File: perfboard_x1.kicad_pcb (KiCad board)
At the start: 2 copper layers, 107.1 x 81.3 mm, 121 parts, among them J1 Conn_01x10, J10 Conn_01x10, J100 Conn_01x10, J101 Conn_01x10, J102 Conn_01x10, J103 Conn_01x10, J104 Conn_01x10, J105 Conn_01x10, J106 Conn_01x10, J107 Conn_01x10, J108 Conn_01x10, J109 Conn_01x10, J11 Conn_01x10, J110 Conn_01x10, J111 Conn_01x10, J112 Conn_01x10, J113 Conn_01x10, J114 Conn_01x10, J115 Conn_01x10, J116 Conn_01x10, J117 Conn_01x10, J118 Conn_01x10, J119 Conn_01x10, J12 Conn_01x10, J120 Conn_01x10, J13 Conn_01x10, J14 Conn_01x10, J15 Conn_01x10, J16 Conn_01x10, J17 Conn_01x10, J18 Conn_01x10, J19 Conn_01x10, J2 Conn_01x10, J20 Conn_01x10, J21 Conn_01x10, J22 Conn_01x10, J23 Conn_01x10, J24 Conn_01x10, J25 Conn_01x10, J26 Conn_01x10, J27 Conn_01x10, J28 Conn_01x10, J29 Conn_01x10, J3 Conn_01x10, J30 Conn_01x10, J31 Conn_01x10, J32 Conn_01x10, J33 Conn_01x10, J34 Conn_01x10, J35 Conn_01x10, J36 Conn_01x10, J37 Conn_01x10, J38 Conn_01x10, J39 Conn_01x10, J4 Conn_01x10, J40 Conn_01x10, J41 Conn_01x10, J42 Conn_01x10, J43 Conn_01x10, J44 Conn_01x10, J45 Conn_01x10, J46 Conn_01x10, J47 Conn_01x10, J48 Conn_01x10, J49 Conn_01x10, J5 Conn_01x10, J50 Conn_01x10, J51 Conn_01x10, J52 Conn_01x10, J53 Conn_01x10, J54 Conn_01x10, J55 Conn_01x10, J56 Conn_01x10, J57 Conn_01x10, J58 Conn_01x10, J59 Conn_01x10, J6 Conn_01x10, J60 Conn_01x10, J61 Conn_01x10, J62 Conn_01x10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

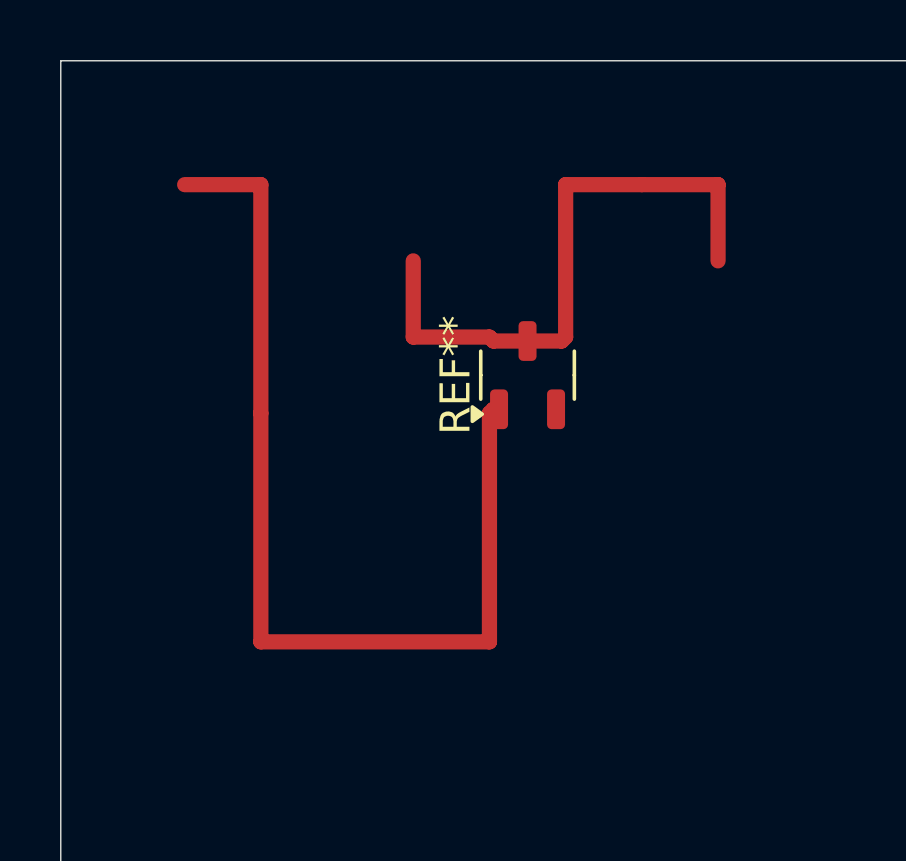
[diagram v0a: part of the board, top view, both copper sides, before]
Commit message: Added a sample circuit
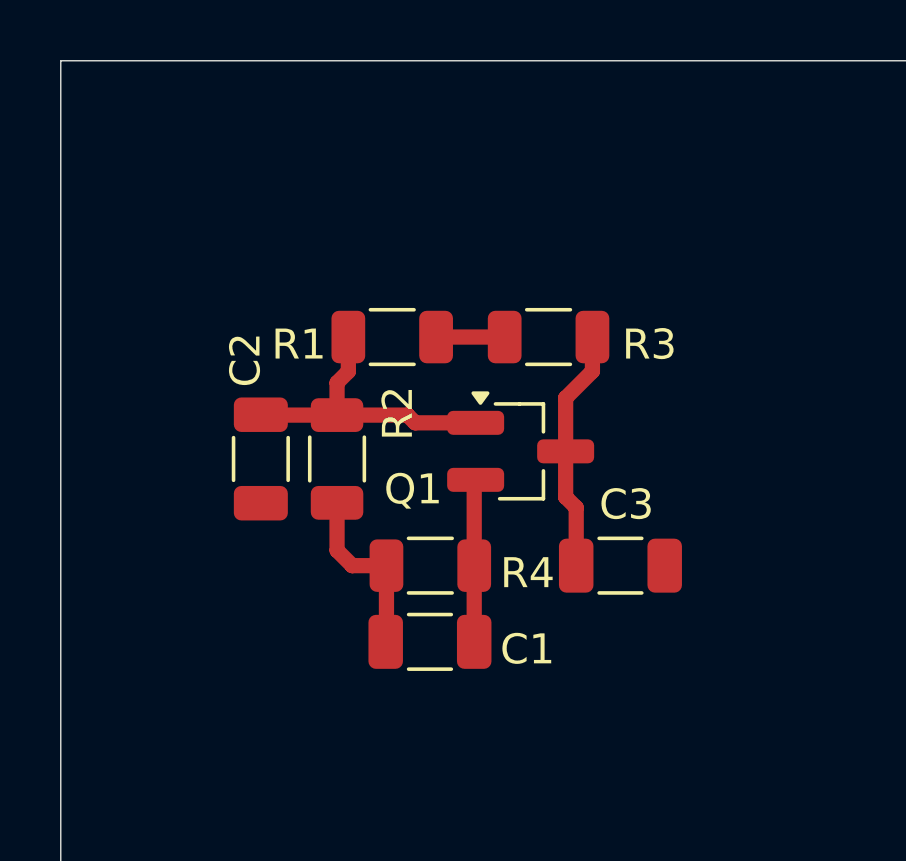
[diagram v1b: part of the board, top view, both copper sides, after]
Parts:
- removed REF**: SOT-23-3, Package_TO_SOT_SMD:SOT-23-3
- added C1: C, Capacitor_SMD:C_1206_3216Metric, F.Cu at (32.3, 39.4)
- added C2: C, Capacitor_SMD:C_1206_3216Metric, F.Cu at (26.7, 33.3)
- added C3: C, Capacitor_SMD:C_1206_3216Metric, F.Cu at (38.7, 36.8)
- added Q1: S8050_smd, aadhunix:SOT-23_alternate_handsoldering, F.Cu at (35.3, 33.0)
- added R1: R, Resistor_SMD:R_1206_3216Metric, F.Cu at (31.0, 29.2)
- added R2: R, Resistor_SMD:R_1206_3216Metric, F.Cu at (29.2, 33.3)
- added R3: R, Resistor_SMD:R_1206_3216Metric, F.Cu at (36.3, 29.2)
- added R4: R, Resistor_SMD:R_1206_3216Metric, F.Cu at (32.3, 36.8)
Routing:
- net (no net): track 53.8 -> 0.00 mm
- net Net-(Q1-B): track 0.00 -> 10.0 mm
- net Net-(Q1-C): track 0.00 -> 8.14 mm
- net GND: track 0.00 -> 5.99 mm
- net Net-(Q1-E): track 0.00 -> 5.42 mm
- net VCC: track 0.00 -> 2.29 mm
